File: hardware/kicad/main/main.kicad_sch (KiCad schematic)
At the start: 17 parts, among them J1 USB_C_Receptacle_USB2.0, J2 SERVO_L, J3 SERVO_R, J4 EXP_FRONT, J5 EXP_BACK, J6 ENC_LEFT, J7 ENC_RIGHT, U1 CH340G, U2 ESP32-WROOM-32, U3 ITR8307, U4 LM339, U5 IP5306

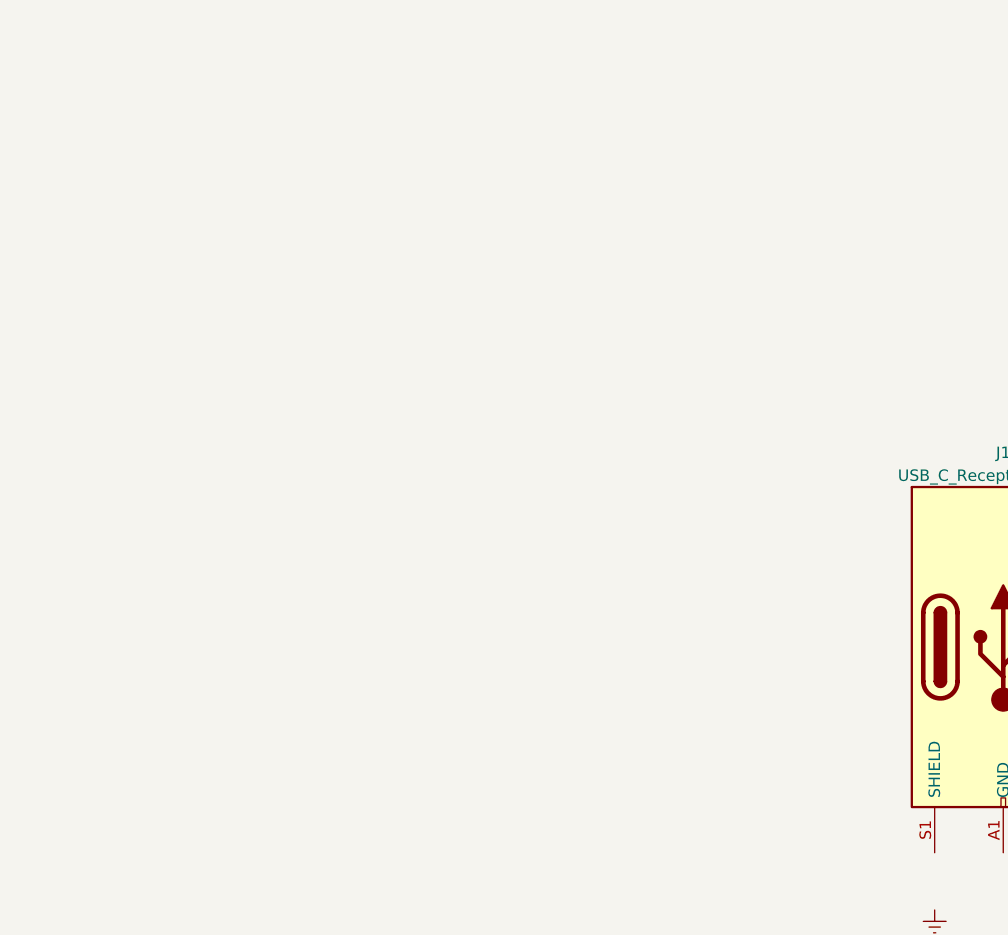
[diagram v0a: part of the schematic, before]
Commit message: used espressif library
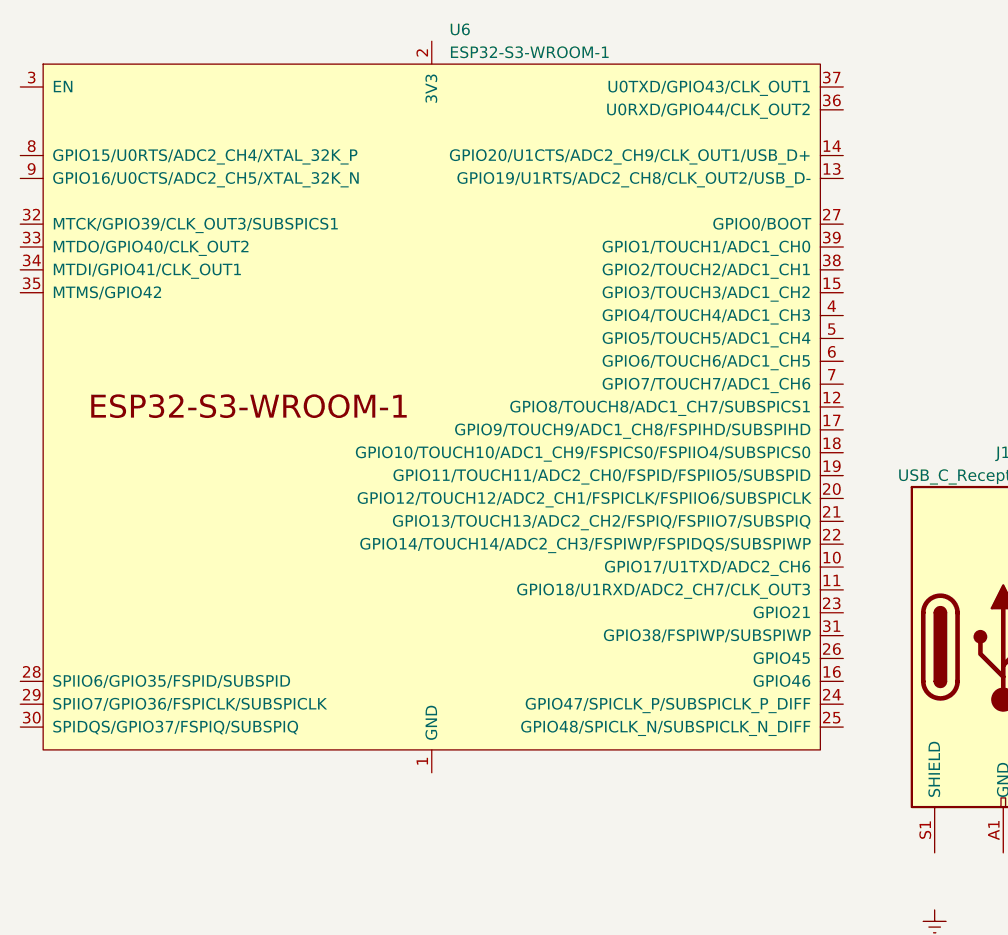
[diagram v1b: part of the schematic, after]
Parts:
- added U6: ESP32-S3-WROOM-1, Espressif:ESP32-S3-WROOM-1, symbol Espressif:ESP32-S3-WROOM-1
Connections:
- new net: U6.1 (GND), U6.40 (GND), U6.41 (GND)
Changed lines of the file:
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@@
+    )
+  )
+  (symbol (lib_id "Espressif:ESP32-S3-WROOM-1") (at -3.81 44.45 0) (unit 1)
+    (in_bom yes) (on_board yes) (dnp no) (fields_autoplaced)
+    (property "Reference" "U6" (at -1.8541 2.54 0)
+      (effects (font (size 1.27 1.27)) (justify left))
+    )
+    (property "Value" "ESP32-S3-WROOM-1" (at -1.8541 5.08 0)
+      (effects (font (size 1.27 1.27)) (justify left))
+    )
+    (property "Footprint" "Espressif:ESP32-S3-WROOM-1" (at -1.27 92.71 0)
+      (effects (font (size 1.27 1.27)) hide)
+    )
+    (property "Datasheet" "https://www.espressif.com/sites/default/files/documentation/esp32-s3-wroom-1_wroom-1u_datasheet_en.pdf" (at -1.27 95.25 0)
+      (effects (font (size 1.27 1.27)) hide)
+    )
+    (pin "1")
+    (pin "10")
+    (pin "11")
+    (pin "12")
+    (pin "13")
+    (pin "14")
+    (pin "15")
+    (pin "16")
+    (pin "17")
+    (pin "18")
+    (pin "19")
+    (pin "2")
+    (pin "20")
+    (pin "21")
+    (pin "22")
+    (pin "23")
+    (pin "24")
+    (pin "25")
+    (pin "26")
+    (pin "27")
+    (pin "28")
+    (pin "29")
+    (pin "3")
+    (pin "30")
+    (pin "31")
+    (pin "32")
+    (pin "33")
+    (pin "34")
+    (pin "35")
+    (pin "36")
+    (pin "37")
+    (pin "38")
+    (pin "39")
+    (pin "4")
+    (pin "40")
+    (pin "41")
+    (pin "5")
+    (pin "6")
+    (pin "7")
+    (pin "8")
+    (pin "9")
+    (instances
+      (project "main"
+        (path "/82f3a3ad-aa6d-4130-9491-8400c82a7c01"
+          (reference "U6") (unit 1)
+        )
+      )
     )
   )

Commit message: most of the routing done, left power supplies and navigation leds
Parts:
- removed A1: Adafruit_Feather_Generic, Module:Adafruit_Feather, symbol MCU_Module:Adafruit_Feather_Generic
- removed J4: EXP_FRONT, Connector_PinSocket_2.54mm:PinSocket_1x10_P2.54mm_Horizontal, symbol Connector:Conn_01x10_Socket
- removed J5: EXP_BACK, Connector_PinSocket_2.54mm:PinSocket_1x10_P2.54mm_Horizontal, symbol Connector:Conn_01x10_Socket
- removed J6: ENC_LEFT, Connector_PinSocket_2.54mm:PinSocket_1x04_P2.54mm_Horizontal, symbol Connector:Conn_01x04_Socket
- removed J7: ENC_RIGHT, Connector_PinSocket_2.54mm:PinSocket_1x04_P2.54mm_Horizontal, symbol Connector:Conn_01x04_Socket
- removed U1: CH340G, Package_SO:SOIC-16_3.9x9.9mm_P1.27mm, symbol Interface_USB:CH340G
- removed U2: ESP32-WROOM-32, RF_Module:ESP32-WROOM-32, symbol RF_Module:ESP32-WROOM-32
- removed U3: ITR8307, OptoDevice:Everlight_ITR8307, symbol Sensor_Proximity:ITR8307
- removed U4: LM339, Package_SO:SOIC-14_3.9x8.7mm_P1.27mm, symbol Comparator:LM339
- added C1, C11, C13, C14, C15, C2, C3, C4, C5, C6, C7, C8, C9: 22u, Capacitor_SMD:C_1206_3216Metric, symbol Device:C
- added C10, C12: 100n, Capacitor_SMD:C_0603_1608Metric, symbol Device:C
- added D1, D2, D3: LESD5D5, Diode_SMD:D_SOD-523, symbol Device:D_TVS
- added D4, D5, D6, D7: W, LED_SMD:LED_0603_1608Metric, symbol Device:LED
- added J10: ENC_LEFT, Connector_PinHeader_2.54mm:PinHeader_1x06_P2.54mm_Horizontal, symbol Connector:Conn_01x06_Pin
- added J11: ENC_RIGHT, Connector_PinHeader_2.54mm:PinHeader_1x06_P2.54mm_Horizontal, symbol Connector:Conn_01x06_Pin
- added J12: UART0, Connector_PinHeader_2.54mm:PinHeader_2x03_P2.54mm_Vertical, symbol Connector_Generic:Conn_02x03_Odd_Even
- added J8: Conn_02x10_Odd_Even, Connector_PinSocket_2.54mm:PinSocket_2x10_P2.54mm_Vertical, symbol Connector_Generic:Conn_02x10_Odd_Even
- added L1: L, Inductor_SMD:L_6.3x6.3_H3, symbol Device:L
- added Q1: 2N7002K, Package_TO_SOT_SMD:SOT-23, symbol Transistor_FET:2N7002K
- added R1, R2, R7: 5k1, Resistor_SMD:R_0603_1608Metric, symbol Device:R
- added R10, R5, R6, R8: 10k, Resistor_SMD:R_0603_1608Metric, symbol Device:R
- added R3, R4: 1R, Resistor_SMD:R_0603_1608Metric, symbol Device:R
- added SW1, SW2, SW3, SW4: SW_SPST, Button_Switch_SMD:SW_SPST_CK_RS282G05A3, symbol Switch:SW_SPST
- added U2: AP1117-33, Package_TO_SOT_SMD:SOT-223-3_TabPin2, symbol Regulator_Linear:AP1117-33
- BT1: value Battery_Cell -> 18650
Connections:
- net +3.3V: now also U6.2 (3V3), C10.1, C11.1, C13.1, C3.1, C8.1, C9.1, J10.2 (Pin_2), J11.2 (Pin_2), J12.6 (Pin_6), J8.3 (Pin_3), Q1.1 (G), R10.1, R6.1, U2.2 (VO)
- net +5V: now also J2.2 (Pin_2), J3.2 (Pin_2), U5.8 (VOUT), C14.1, C15.1, C4.1, C5.1, C6.1, J8.2 (Pin_2), U2.3 (VI)
- net GND: now also BT1.2 (-), J1.A1 (GND), J1.A12 (GND), J1.B1 (GND), J1.B12 (GND), J1.S1 (SHIELD), J2.3 (Pin_3), J3.3 (Pin_3), U5.9 (GND), U6.1 (GND), U6.40 (GND), U6.41 (GND), C1.2, C10.2, C11.2, C12.2, C13.2, C14.2, C15.2, C2.2, C3.2, C4.2, C5.2, C6.2, C7.2, C8.2, C9.2, D1.1 (A1), D2.1 (A1), D3.1 (A1), J10.1 (Pin_1), J11.1 (Pin_1), J12.5 (Pin_5), J8.1 (Pin_1), Q1.2 (S), R1.2, R10.2, R2.2, SW1.2 (B), SW2.1 (A), U2.1 (GND)
- net at BT1.1 (+): now also C2.1, L1.2, R3.1, R7.2
- net +5VD: now reaches U5.1 (VIN)
- net +5VD: now also J1.A4 (VBUS), J1.A9 (VBUS), J1.B4 (VBUS), J1.B9 (VBUS), D1.2 (A2), R4.1
- net at U5.2 (LED1): now also D4.2 (A), D5.1 (K)
- net at U5.3 (LED2): now also D6.2 (A), D7.1 (K)
- net at U5.4 (LED3): now also D4.1 (K), D5.2 (A), D6.1 (K), D7.2 (A)
- net at U5.5 (KEY): now also R5.1
- net at U5.6 (BAT): now also C1.1, R3.2
- net at U5.7 (SW): now also L1.1
- net GPIO16: now reaches J3.1 (Pin_1)
- net GPIO16: now also U6.9 (GPIO16/U0CTS/ADC2_CH5/XTAL_32K_N)
- net GPIO15: now reaches J2.1 (Pin_1)
- net GPIO15: now also U6.8 (GPIO15/U0RTS/ADC2_CH4/XTAL_32K_P)
- net UART1_TX: now reaches U6.10 (GPIO17/U1TXD/ADC2_CH6)
- net UART1_TX: now also J8.6 (Pin_6)
- net UART1_RX: now reaches U6.11 (GPIO18/U1RXD/ADC2_CH7/CLK_OUT3)
- net UART1_RX: now also J8.4 (Pin_4)
- net GPIO8: now reaches U6.12 (GPIO8/TOUCH8/ADC1_CH7/SUBSPICS1)
- net GPIO8: now also J11.3 (Pin_3)
- net USB_D-: now reaches U6.13 (GPIO19/U1RTS/ADC2_CH8/CLK_OUT2/USB_D-)
- net USB_D-: now also J1.A7 (D-), J1.B7 (D-), D2.2 (A2)
- net USB_D+: now reaches U6.14 (GPIO20/U1CTS/ADC2_CH9/CLK_OUT1/USB_D+)
- net USB_D+: now also J1.A6 (D+), J1.B6 (D+), D3.2 (A2)
- net STRAP3: now reaches U6.15 (GPIO3/TOUCH3/ADC1_CH2)
- net STRAP3: now also J11.6 (Pin_6)
- net STRAP46: now reaches U6.16 (GPIO46)
- net STRAP46: now also J11.5 (Pin_5)
- net GPIO9/ADC1_8: now reaches U6.17 (GPIO9/TOUCH9/ADC1_CH8/FSPIHD/SUBSPIHD)
- net GPIO9/ADC1_8: now also J8.8 (Pin_8)
- net GPIO10/ADC1_9: now reaches U6.18 (GPIO10/TOUCH10/ADC1_CH9/FSPICS0/FSPIIO4/SUBSPICS0)
- net GPIO10/ADC1_9: now also J8.5 (Pin_5)
- net GPIO11: now reaches U6.19 (GPIO11/TOUCH11/ADC2_CH0/FSPID/FSPIIO5/SUBSPID)
- net GPIO11: now also J11.4 (Pin_4)
- net GPIO12: now reaches U6.20 (GPIO12/TOUCH12/ADC2_CH1/FSPICLK/FSPIIO6/SUBSPICLK)
- net GPIO12: now also J8.7 (Pin_7)
- net GPIO13: now reaches U6.21 (GPIO13/TOUCH13/ADC2_CH2/FSPIQ/FSPIIO7/SUBSPIQ)
- net GPIO13: now also J8.10 (Pin_10)
- net GPIO14: now reaches U6.22 (GPIO14/TOUCH14/ADC2_CH3/FSPIWP/FSPIDQS/SUBSPIWP)
- net GPIO14: now also J8.9 (Pin_9)
- net GPIO21: now reaches U6.23 (GPIO21)
- net GPIO21: now also J8.12 (Pin_12)
- net GPIO47: now reaches U6.24 (GPIO47/SPICLK_P/SUBSPICLK_P_DIFF)
- net GPIO47: now also J8.11 (Pin_11)
- net GPIO48: now reaches U6.25 (GPIO48/SPICLK_N/SUBSPICLK_N_DIFF)
- net GPIO48: now also J8.14 (Pin_14)
- net STRAP45: now reaches U6.26 (GPIO45)
- net STRAP45: now also J10.5 (Pin_5)
- net STRAP0: now reaches U6.27 (GPIO0/BOOT)
- net STRAP0: now also J12.2 (Pin_2), SW4.2 (B)
- net PSRAM_35: now reaches U6.28 (SPIIO6/GPIO35/FSPID/SUBSPID)
- net PSRAM_36: now reaches U6.29 (SPIIO7/GPIO36/FSPICLK/SUBSPICLK)
- net ~{RST}: now reaches U6.3 (EN)
- net ~{RST}: now also C12.1, J12.3 (Pin_3), R6.2, SW2.2 (B)
- net PSRAM_37: now reaches U6.30 (SPIDQS/GPIO37/FSPIQ/SUBSPIQ)
- net GPIO38: now reaches U6.31 (GPIO38/FSPIWP/SUBSPIWP)
- net GPIO38: now also J8.13 (Pin_13)
- net GPIO39: now reaches U6.32 (MTCK/GPIO39/CLK_OUT3/SUBSPICS1)
- net GPIO39: now also J8.16 (Pin_16)
- net GPIO40: now reaches U6.33 (MTDO/GPIO40/CLK_OUT2)
- net GPIO41: now reaches U6.34 (MTDI/GPIO41/CLK_OUT1)
- net GPIO42: now reaches U6.35 (MTMS/GPIO42)
- net UART0_RX: now reaches U6.36 (U0RXD/GPIO44/CLK_OUT2)
- net UART0_RX: now also J12.4 (Pin_4)
- net UART0_TX: now reaches U6.37 (U0TXD/GPIO43/CLK_OUT1)
- net UART0_TX: now also J12.1 (Pin_1)
- net GPIO2/ADC1_1: now reaches U6.38 (GPIO2/TOUCH2/ADC1_CH1)
- net GPIO2/ADC1_1: now also J8.15 (Pin_15)
- net GPIO1/ADC1_0: now reaches U6.39 (GPIO1/TOUCH1/ADC1_CH0)
- net GPIO1/ADC1_0: now also J8.17 (Pin_17)
- net GPIO4: now reaches U6.4 (GPIO4/TOUCH4/ADC1_CH3)
- net GPIO4: now also J10.3 (Pin_3)
- net GPIO5: now reaches U6.5 (GPIO5/TOUCH5/ADC1_CH4)
- net GPIO5: now also J10.4 (Pin_4)
- net GPIO6: now reaches U6.6 (GPIO6/TOUCH6/ADC1_CH5)
- net GPIO6: now also J10.6 (Pin_6)
- net GPIO7/ADC1_6: now reaches U6.7 (GPIO7/TOUCH7/ADC1_CH6)
- net GPIO7/ADC1_6: now also R7.1, R8.1
- net at J1.A5 (CC1): now also R1.1
- net at J1.A8 (SBU1): now also J1.B8 (SBU2)
- net at J1.B5 (CC2): now also R2.1
- new net: C7.1, R4.2
- new net: R5.2, SW1.1 (A)
- new net: Q1.3 (D), R8.2
- no-connect marks 0 -> 6
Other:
- note added: "strap0 - boot mode, must be button input"
- note added: "strap3 - jtag source, can be hi-z output"
- note added: "strap45 - spi voltage, can be hi-z output"
- note added: "strap46 - boot log, can be hi-z output"
- note removed: "IP5306 battery management ic"
- company: (none) -> kabot.io
- title: (none) -> Kabot main board
- moved on the sheet: BT1, H1, H2, H3, J1, J2, J3, U5, U6

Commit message: routing pretty much done, passing DRC
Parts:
- added D10: G, LED_SMD:LED_0603_1608Metric, symbol Device:LED
- added D11: B, LED_SMD:LED_0603_1608Metric, symbol Device:LED
- added D8: SK6812MINI, LED_SMD:LED_SK6812MINI_PLCC4_3.5x3.5mm_P1.75mm, symbol LED:SK6812MINI
- added D9: R, LED_SMD:LED_0603_1608Metric, symbol Device:LED
- added H4: MountingHole_Pad, MountingHole:MountingHole_3.2mm_M3_DIN965_Pad, symbol Mechanical:MountingHole_Pad
- added J4: Conn_01x02_Pin, Connector_PinHeader_2.54mm:PinHeader_1x02_P2.54mm_Horizontal, symbol Connector:Conn_01x02_Pin
- added R11, R12, R9: 1k, Resistor_SMD:R_0603_1608Metric, symbol Device:R
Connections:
- net +3.3V: now also J10.5 (Pin_5), J11.5 (Pin_5), J12.2 (Pin_2), D8.4 (VDD); no longer J10.2 (Pin_2), J11.2 (Pin_2), J12.6 (Pin_6)
- net GND: now also H1.1, H2.1, H3.1, J10.6 (Pin_6), J11.6 (Pin_6), J12.1 (Pin_1), J2.1 (Pin_1), J3.1 (Pin_1), SW3.1 (A), SW4.1 (A), D10.1 (K), D11.1 (K), D8.2 (VSS), D9.1 (K), H4.1, J4.1 (Pin_1); no longer BT1.2 (-), J10.1 (Pin_1), J11.1 (Pin_1), J12.5 (Pin_5), J2.3 (Pin_3), J3.3 (Pin_3)
- net GPIO15: now also J2.3 (Pin_3); no longer J2.1 (Pin_1)
- net GPIO16: now also J3.3 (Pin_3); no longer J3.1 (Pin_1)
- net GPIO4: now also J10.4 (Pin_4); no longer J10.3 (Pin_3)
- net GPIO40: now also R11.1, R12.1, R9.1
- net GPIO41: now also D8.3 (DIN)
- net GPIO42: now also SW3.2 (B)
- net GPIO5: now also J10.3 (Pin_3); no longer J10.4 (Pin_4)
- net GPIO6: now also J10.1 (Pin_1); no longer J10.6 (Pin_6)
- net STRAP0: now also J12.6 (Pin_6); no longer J12.2 (Pin_2)
- net STRAP3: now also J11.1 (Pin_1); no longer J11.6 (Pin_6)
- net STRAP45: now also J10.2 (Pin_2); no longer J10.5 (Pin_5)
- net STRAP46: now also J11.2 (Pin_2); no longer J11.5 (Pin_5)
- net UART0_TX: now also J12.5 (Pin_5); no longer J12.1 (Pin_1)
- net at C2.1, L1.2, R3.1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: now also J4.2 (Pin_2); no longer BT1.1 (+)
- new net: D10.2 (A), R11.2
- new net: D11.2 (A), R12.2
- new net: D9.2 (A), R9.2
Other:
- moved on the sheet: BT1, C1, C10, C11, C12, C13, C14, C15, C2, C3, C4, C5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
